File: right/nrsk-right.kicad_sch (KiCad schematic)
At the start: 125 parts, among them J1 PJ-320D, J2 USB-C, J3 OLED 128x32, SW1 71, SW10 8, SW11 9, SW12 0, SW13 -, SW14 =, SW15 Backspace, SW16 75, SW17 Y, SW18 U, SW19 I, SW2 F7, SW20 O, SW21 P, SW22 [, SW23 ], SW24 \, SW25 77, SW26 H, SW27 J, SW28 K, SW29 L, SW3 F8, SW30 ;, SW31 ', SW32 Enter, SW33 79, SW34 N, SW35 M, SW36 ,, SW37 ., SW38 /, SW39 ↑, SW4 F9, SW40 fn, SW41 81, SW42 Space, SW43 Space, SW44 Cmd, SW45 Opt, SW46 ←, SW47 ↓, SW48 →, SW5 F10, SW6 F11, SW7 F12, SW8 73, SW9 7, U1 ATmega32U4-AU, U2 USBLC6-2SC6, U3 AS5600-ASOM, Y1 16MHz

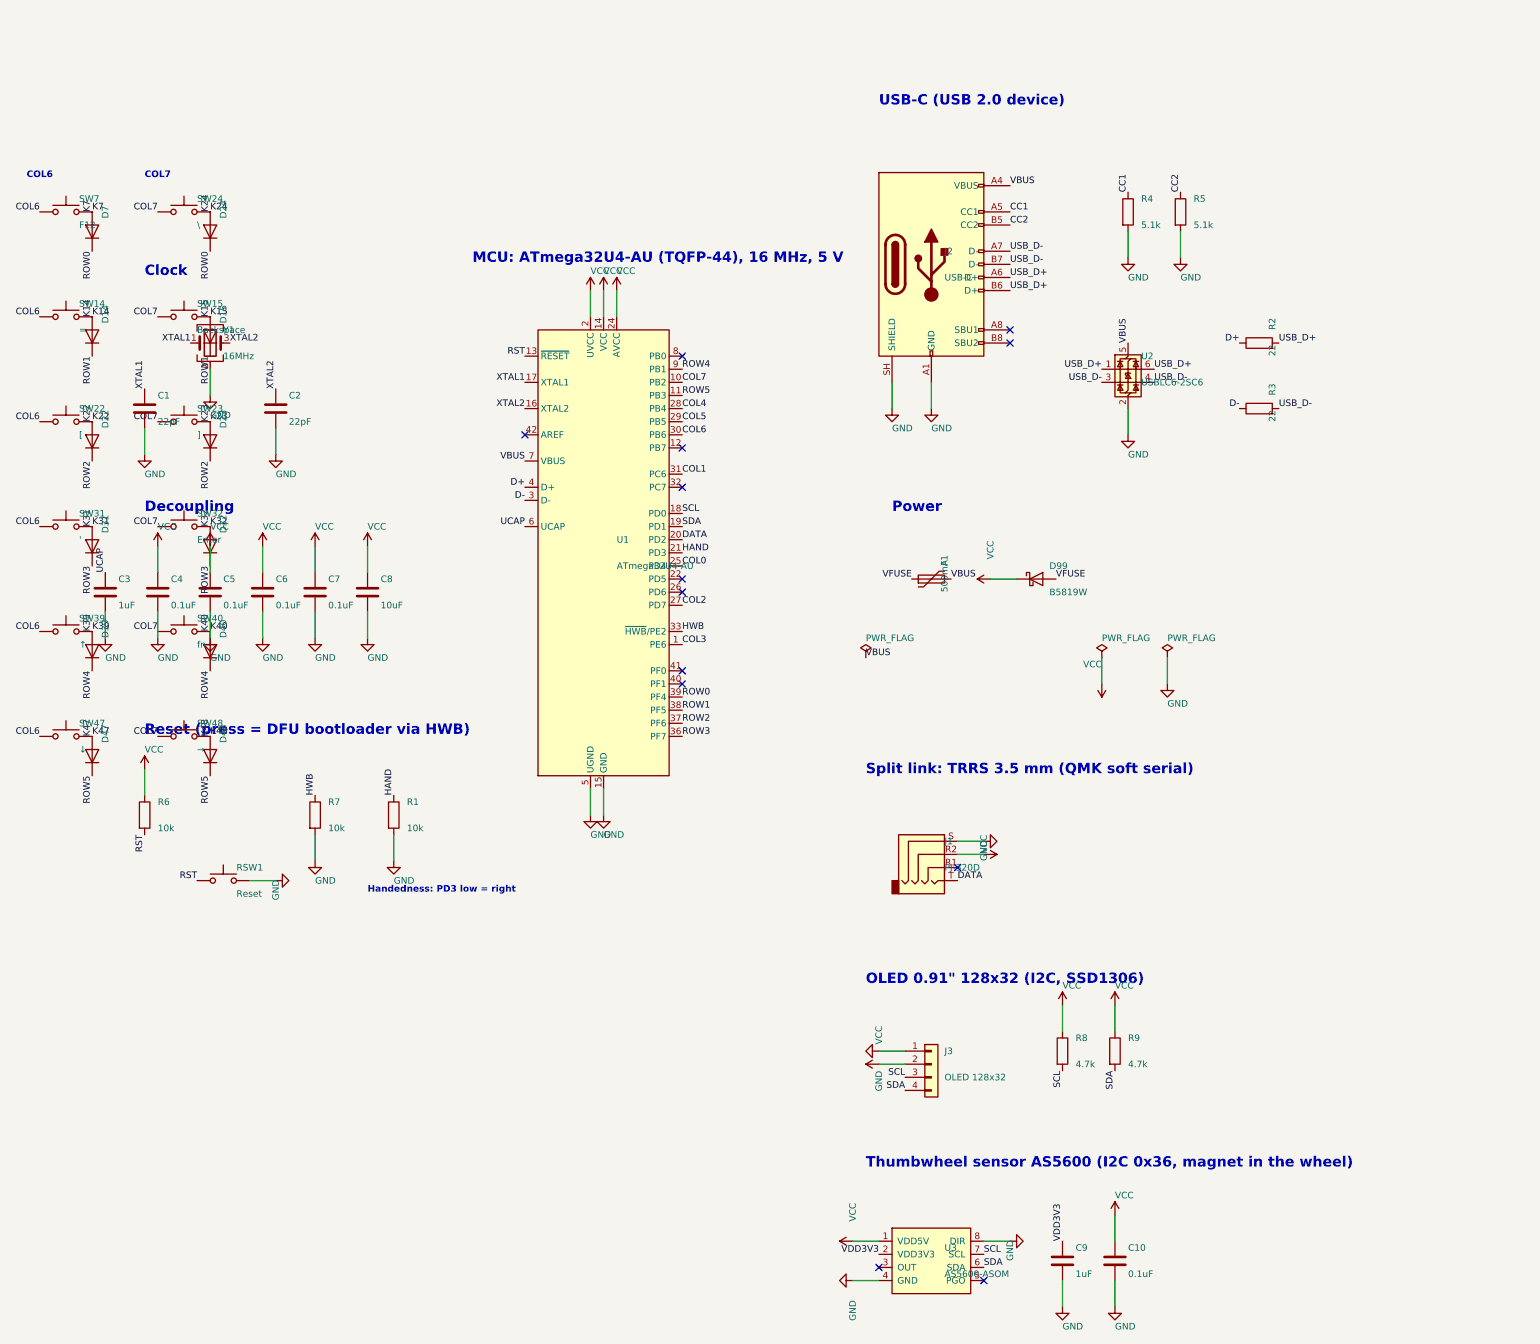
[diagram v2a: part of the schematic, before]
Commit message: Move to RP2040, rework OLED/connectors/wheel, add all-printed case and assembly guide
- MCU: RP2040 + W25Q128JV + 12 MHz crystal + AP2112K 3.3 V LDO on each half;
  QMK config for RP2040 (UF2, PIO serial, I2C1 on GP2/GP3); routing helped by
  MCU escape stubs, TESTEN-to-pad stub, exposed-pad vias and a fan-out ring
- Boards: top edge +5 mm, inner edges widened; USB-C on the back edge, TRRS
  behind the OLED at the same height on both halves
- OLED: half-mirror acrylic (2 mm) rounded rectangle centred on the display,
  flush with the plate, held by double-sided tape
- Wheel: 32 rim teeth + M3 ball plunger for detents; removable corner cap so
  the printed tray can be assembled; magnet shown in viewer
- Case variants: A (printed tray + clear acrylic plate), B (all printed, plate
  with stiffening web), acrylic stack; slim-head M2 plate screws; tray fillets
- Viewer: shared model-data.js, wheel toggle, rotate below; new interactive
  assembly guide (case/preview/assembly.html, also on Pages)
- BOM: RP2040 parts, plunger, slim-head screws, acrylic finishes, all with
  verified sources; README and renders updated

Co-Authored-By: Claude Opus 5.5 <noreply@anthropic.com>
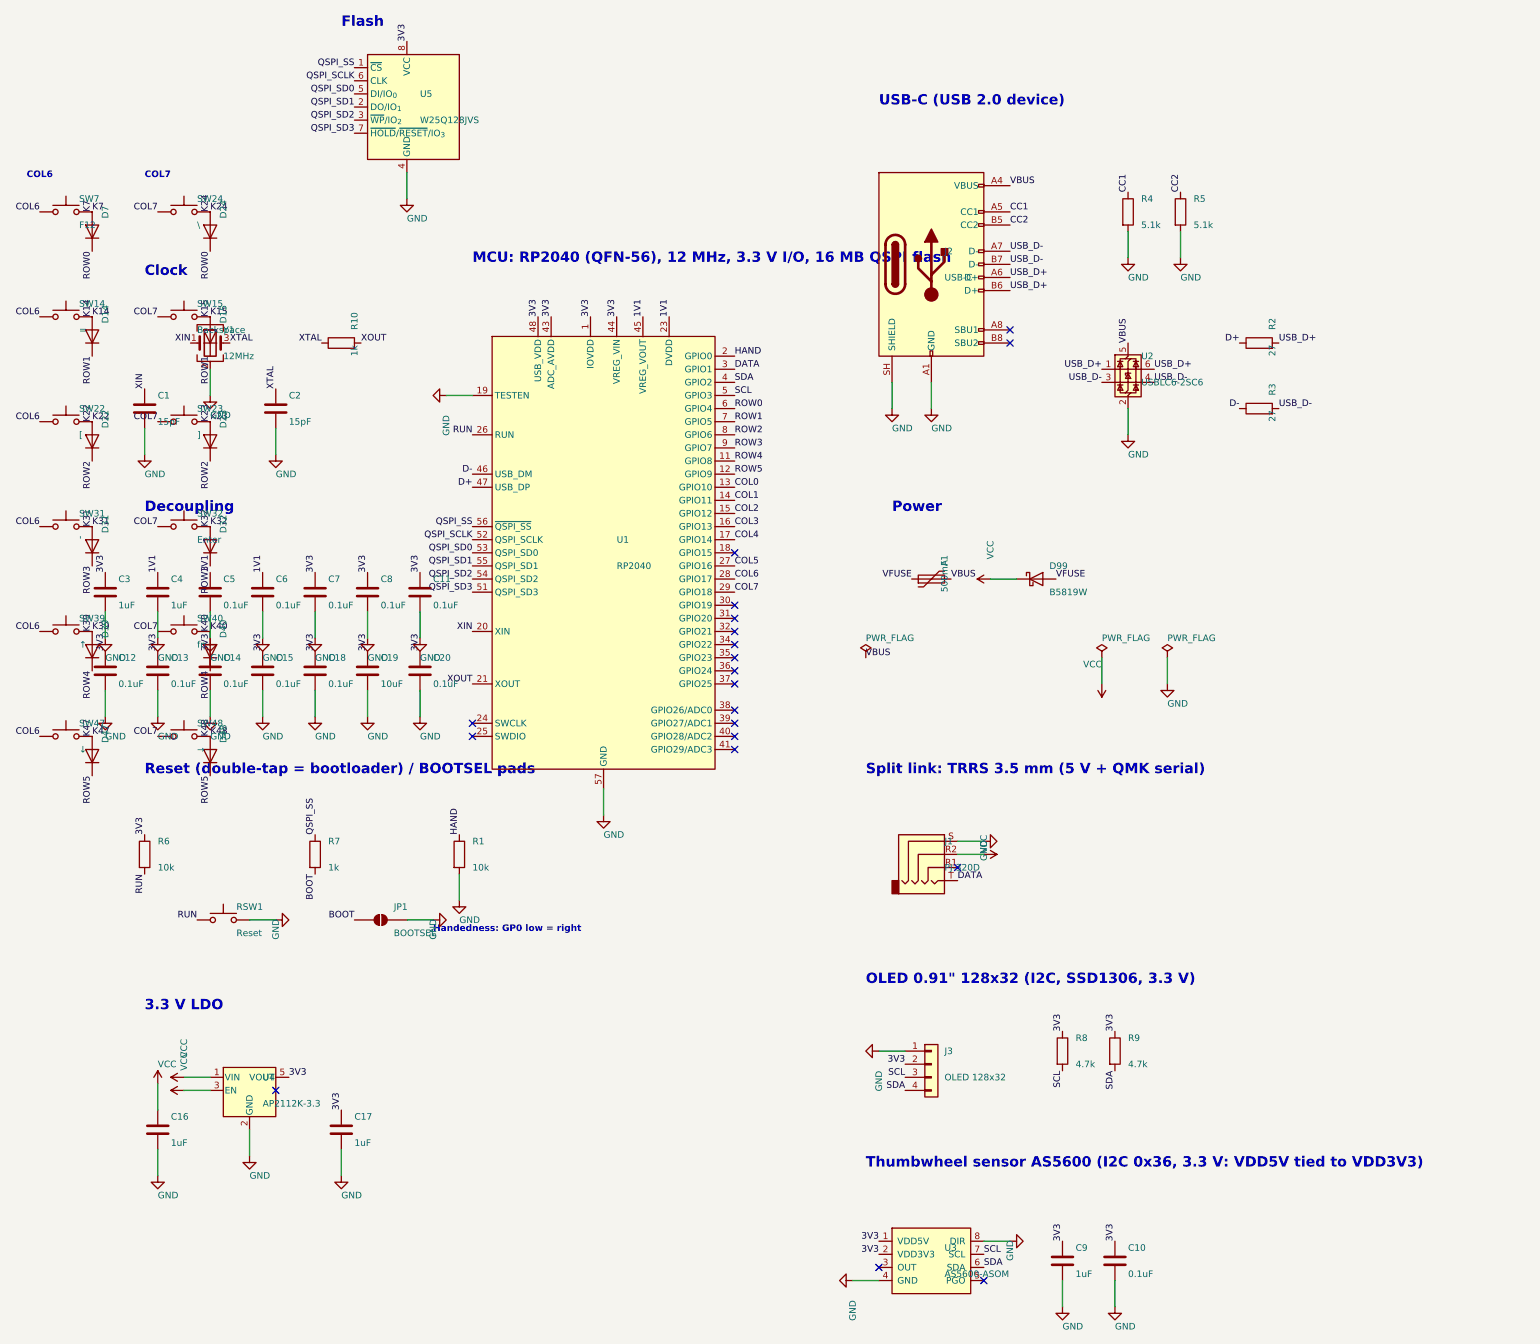
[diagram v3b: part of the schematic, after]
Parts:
- added C11, C12, C13, C14, C15, C18, C20: 0.1uF, Capacitor_SMD:C_0805_2012Metric, symbol Device:C
- added C16, C17: 1uF, Capacitor_SMD:C_0805_2012Metric, symbol Device:C
- added C19: 10uF, Capacitor_SMD:C_0805_2012Metric, symbol Device:C
- added JP1: BOOTSEL, Jumper:SolderJumper-2_P1.3mm_Open_RoundedPad1.0x1.5mm, symbol Jumper:SolderJumper_2_Open
- added R10: 1k, Resistor_SMD:R_0805_2012Metric, symbol Device:R
- added U4: AP2112K-3.3, Package_TO_SOT_SMD:SOT-23-5, symbol Regulator_Linear:AP2112K-3.3
- added U5: W25Q128JVS, Package_SO:SOIC-8_5.3x5.3mm_P1.27mm, symbol Memory_Flash:W25Q128JVS
- C1, C2: value 22pF -> 15pF
- C4: value 0.1uF -> 1uF
- C8: value 10uF -> 0.1uF
- R2, R3: value 22 -> 27
- R7: value 10k -> 1k
- U1: value ATmega32U4-AU -> RP2040; footprint Package_QFP:TQFP-44_10x10mm_P0.8mm -> Package_DFN_QFN:QFN-56-1EP_7x7mm_P0.4mm_EP3.2x3.2mm; symbol MCU_Microchip_ATmega:ATmega32U4-A -> MCU_RaspberryPi:RP2040
- Y1: value 16MHz -> 12MHz
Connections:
- net VDD3V3 is gone; now on net 3V3: C9.1, U3.2 (VDD3V3)
- net COL0: now also U1.13 (GPIO10); no longer U1.25 (PD4)
- net COL1: now also U1.14 (GPIO11); no longer U1.31 (PC6)
- net COL2: now also U1.15 (GPIO12); no longer U1.27 (PD7)
- net COL3: now also U1.16 (GPIO13); no longer U1.1 (PE6)
- net COL4: now also U1.17 (GPIO14); no longer U1.28 (PB4)
- net COL5: now also U1.27 (GPIO16); no longer U1.29 (PB5)
- net COL6: now also U1.28 (GPIO17); no longer U1.30 (PB6)
- net D+: now also U1.47 (USB_DP); no longer U1.4 (D+)
- net D-: now also U1.46 (USB_DM); no longer U1.3 (D-)
- net DATA: now also U1.3 (GPIO1); no longer U1.20 (PD2)
- net GND: now also U1.19 (TESTEN), U1.29 (GPIO18), U1.57 (GND), C11.2, C12.2, C13.2, C14.2, C15.2, C16.2, C17.2, C18.2, C19.2, C20.2, JP1.2 (B), U4.2 (GND), U5.4 (GND); no longer R7.2, U1.10 (PB2), U1.15 (GND), U1.23 (GND), U1.35 (GND), U1.43 (GND), U1.5 (UGND)
- net HAND: now also U1.2 (GPIO0); no longer U1.21 (PD3)
- net ROW0: now also U1.6 (GPIO4); no longer U1.39 (PF4)
- net ROW1: now also U1.7 (GPIO5); no longer U1.38 (PF5)
- net ROW2: now also U1.8 (GPIO6); no longer U1.37 (PF6)
- net ROW4: now also U1.11 (GPIO8); no longer U1.9 (PB1)
- net ROW5: now also U1.12 (GPIO9); no longer U1.11 (PB3)
- net SCL: now also U1.5 (GPIO3); no longer U1.18 (PD0)
- net SDA: now also U1.4 (GPIO2); no longer U1.19 (PD1)
- net VBUS: no longer U1.7 (VBUS)
- net VCC: now also C16.1, U4.1 (VIN), U4.3 (EN); no longer C10.1, C4.1, C5.1, C6.1, C7.1, C8.1, D25.1 (K), D26.1 (K), D27.1 (K), D28.1 (K), D29.1 (K), D30.1 (K), D31.1 (K), D32.1 (K), J3.2 (Pin_2), R6.1, R8.1, R9.1, U1.14 (VCC), U1.2 (UVCC), U1.24 (AVCC), U1.34 (VCC), U1.36 (PF7), U1.44 (AVCC), U3.1 (VDD5V)
- net 3V3: now reaches U1.22 (IOVDD)
- net 3V3: now also C10.1, C3.1, C7.1, C8.1, J3.2 (Pin_2), R6.1, R8.1, R9.1, U1.1 (IOVDD), U1.10 (IOVDD), U1.33 (IOVDD), U1.42 (IOVDD), U1.43 (ADC_AVDD), U1.44 (VREG_VIN), U1.48 (USB_VDD), U1.49 (IOVDD), U3.1 (VDD5V), C11.1, C12.1, C13.1, C14.1, C15.1, C17.1, C18.1, C19.1, C20.1, U4.5 (VOUT), U5.8 (VCC)
- net RUN: now reaches U1.26 (RUN)
- net RUN: now also R6.2, RSW1.1
- net HWB renamed QSPI_SS
- net QSPI_SS: now also U1.56 (~{QSPI_SS}), U5.1 (~{CS}); no longer U1.33 (~{HWB}/PE2)
- removed net RST: R6.2, RSW1.1, U1.13 (~{RESET})
- removed net UCAP: C3.1, U1.6 (UCAP)
- net XTAL1 renamed XIN
- net XIN: now also U1.20 (XIN); no longer U1.17 (XTAL1)
- net XTAL2 renamed XTAL
- net XTAL: now also R10.1; no longer U1.16 (XTAL2)
- new net 1V1: C4.1, C5.1, C6.1, U1.23 (DVDD), U1.45 (VREG_VOUT), U1.50 (DVDD)
- new net BOOT: JP1.1 (A), R7.2
- new net QSPI_SCLK: U1.52 (QSPI_SCLK), U5.6 (CLK)
- new net QSPI_SD0: U1.53 (QSPI_SD0), U5.5 (DI/IO_{0})
- new net QSPI_SD1: U1.55 (QSPI_SD1), U5.2 (DO/IO_{1})
- new net QSPI_SD2: U1.54 (QSPI_SD2), U5.3 (~{WP}/IO_{2})
- new net QSPI_SD3: U1.51 (QSPI_SD3), U5.7 (~{HOLD}/~{RESET}/IO_{3})
- new net ROW3: D25.1 (K), D26.1 (K), D27.1 (K), D28.1 (K), D29.1 (K), D30.1 (K), D31.1 (K), D32.1 (K), U1.9 (GPIO7)
- new net XOUT: R10.2, U1.21 (XOUT)
- no-connect marks 13 -> 20
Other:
- note added: "3.3 V LDO"
- note added: "Flash"
- note added: "Handedness: GP0 low = right"
- note added: "MCU: RP2040 (QFN-56), 12 MHz, 3.3 V I/O, 16 MB QSPI flash"
- note added: "OLED 0.91" 128x32 (I2C, SSD1306, 3.3 V)"
- note added: "Reset (double-tap = bootloader) / BOOTSEL pads"
- note added: "Split link: TRRS 3.5 mm (5 V + QMK serial)"
- note added: "Thumbwheel sensor AS5600 (I2C 0x36, 3.3 V: VDD5V tied to VDD3V3)"
- note removed: "Handedness: PD3 low = right"
- note removed: "MCU: ATmega32U4-AU (TQFP-44), 16 MHz, 5 V"
- note removed: "OLED 0.91" 128x32 (I2C, SSD1306)"
- note removed: "Reset (press = DFU bootloader via HWB)"
- note removed: "Split link: TRRS 3.5 mm (QMK soft serial)"
- note removed: "Thumbwheel sensor AS5600 (I2C 0x36, magnet in the wheel)"
- moved on the sheet: R1, R6, R7, RSW1
